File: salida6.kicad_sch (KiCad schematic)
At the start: 7 parts

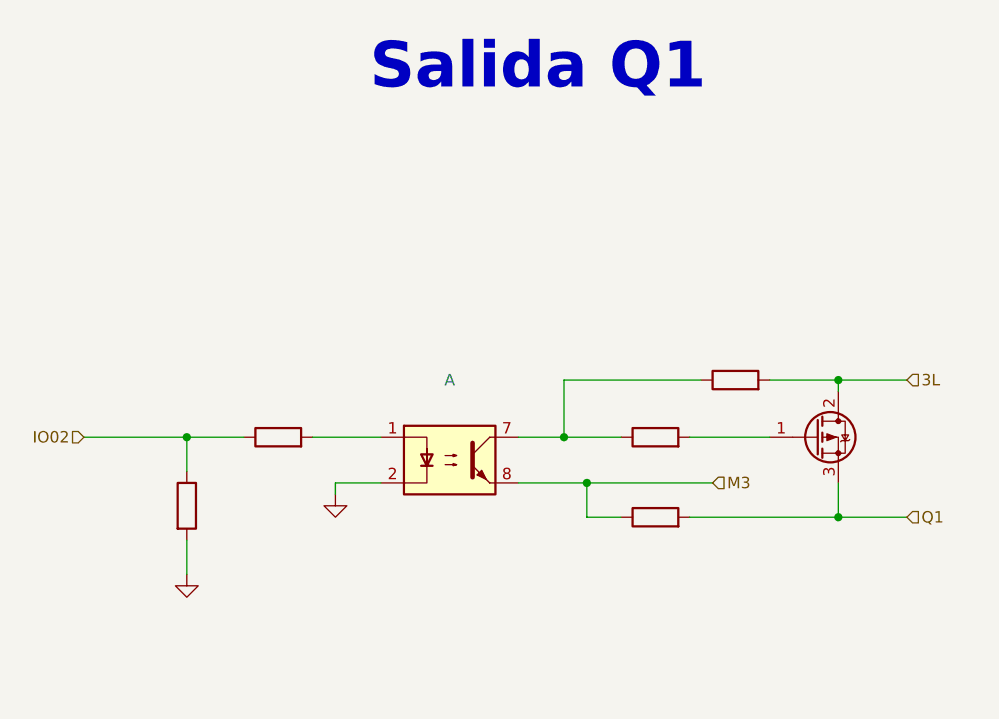
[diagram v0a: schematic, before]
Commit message: add salidas separadas 4,5,6
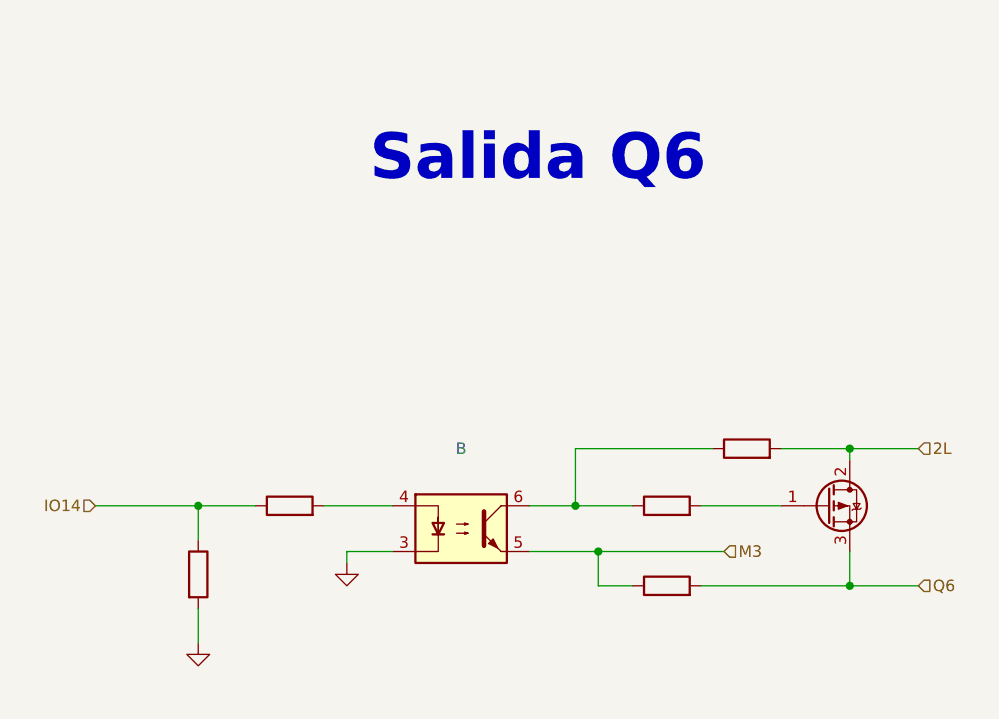
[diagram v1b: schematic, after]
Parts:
- removed ? (x5): (no value), symbol Device:R
- removed ?: (no value), symbol Transistor_FET:FQP27P06
- removed ?: (no value), symbol Isolator:ILD74
- added ? (x5): (no value), symbol Device:R
- added ?: (no value), symbol Isolator:ILD74
- added ?: (no value), symbol Transistor_FET:FQP27P06
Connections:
- net GND: now also ?.2, ?.3
- net M3: now also ?.1, ?.5
- new net: ?.2, ?.4
- new net: ?.1, ?.1, ?.6
- new net: ?.1 (G), ?.2
- new net 2L: ?.2, ?.2 (D)
- new net IO14: ?.1, ?.1
- new net Q6: ?.2, ?.3 (S)
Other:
- note added: "Salida Q6"
- note removed: "Salida Q1"

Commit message: add entradas separadas
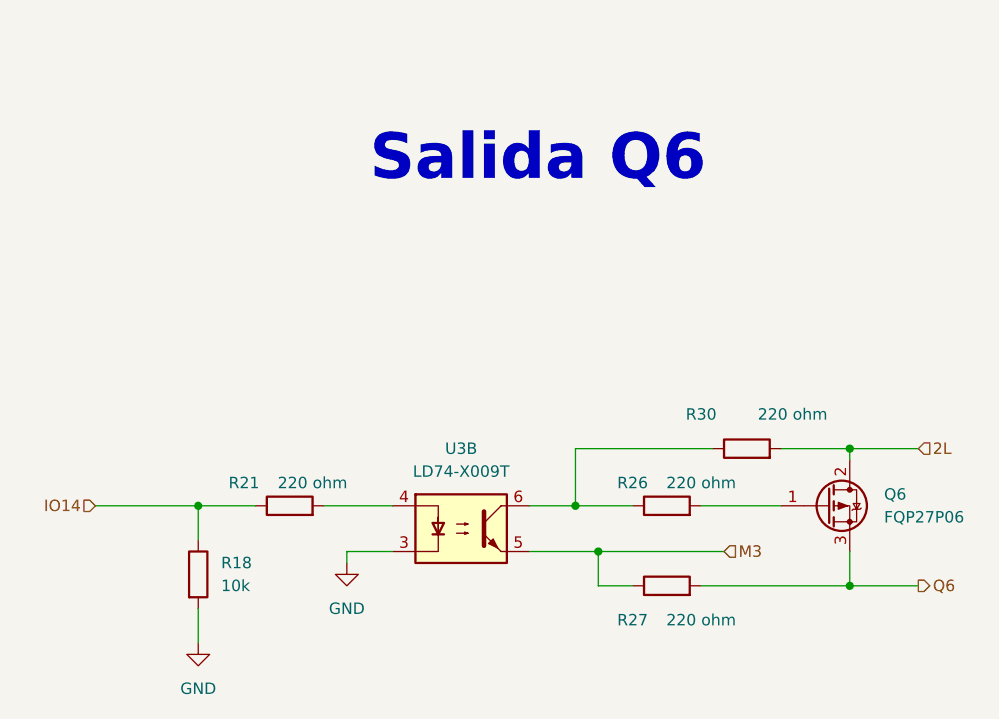
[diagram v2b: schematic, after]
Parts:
- Q6: renamed from ?; value (none) -> FQP27P06; footprint (none) -> Package_TO_SOT_SMD:TO-252-3_TabPin2
- R18: renamed from ?; value (none) -> 10k; footprint (none) -> Resistor_SMD:R_0603_1608Metric
- R21, R26, R27, R30: renamed from ?; value (none) -> 220 ohm; footprint (none) -> Resistor_SMD:R_0603_1608Metric
- U3: renamed from ?; value (none) -> LD74-X009T; footprint (none) -> Package_DIP:DIP-8_W8.89mm_SMDSocket_LongPads
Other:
- title: (none) -> Salida 24 Vdc
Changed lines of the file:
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@@
-(kicad_sch (version 20220929) (generator eeschema)
+(kicad_sch (version 20221004) (generator eeschema)
   (paper "A4" portrait)
+  (title_block
+    (title "Salida 24 Vdc")
+    (date "2022-10-05")
+    (rev "José Luis Laica")
+  )
   (junction (at 142.24 120.65) (diameter 0) (color 0 0 0 0)
   )
@@
     )
   )
-  (hierarchical_label "Q6" (shape input) (at 149.86 135.89 0) (fields_autoplaced)
+  (hierarchical_label "Q6" (shape output) (at 149.86 135.89 0) (fields_autoplaced)
     (effects (font (size 1.27 1.27)) (justify left))
   )
@@
   (symbol (lib_id "Device:R") (at 80.01 127 90) (unit 1)
     (in_bom yes) (on_board yes) (dnp no)
-    (default_instance (reference "") (unit 1) (value "") (footprint ""))
-    (property "Reference" "" (at 74.93 124.46 90)
-      (effects (font (size 1.27 1.27)))
-    )
-    (property "Value" "" (at 82.55 124.46 90)
-      (effects (font (size 1.27 1.27)))
-    )
-    (property "Footprint" "" (at 80.01 128.778 90)
+    (property "Reference" "R21" (at 74.93 124.46 90)
+      (effects (font (size 1.27 1.27)))
+    )
+    (property "Value" "220 ohm" (at 82.55 124.46 90)
+      (effects (font (size 1.27 1.27)))
+    )
+    (property "Footprint" "Resistor_SMD:R_0603_1608Metric" (at 80.01 128.778 90)
       (effects (font (size 1.27 1.27)) hide)
     )
@@
     (pin "1")
     (pin "2")
+    (instances
+      (project "PLC 32 V2"
+        (path "/d17a54f1-6eda-453f-95e1-42a53b02a1c3/4109c560-1e4d-481f-b3b5-bb77ed9700b9"
+          (reference "R21") (unit 1) (value "220 ohm") (footprint "Resistor_SMD:R_0603_1608Metric")
+        )
+      )
+    )
   )
   (symbol (lib_id "Isolator:ILD74") (at 99.06 129.54 0) (unit 2)
     (in_bom yes) (on_board yes) (dnp no) (fields_autoplaced)
-    (default_instance (reference "") (unit 1) (value "") (footprint ""))
-    (property "Reference" "" (at 99.06 120.65 0)
-      (effects (font (size 1.27 1.27)))
-    )
-    (property "Value" "" (at 99.06 123.19 0)
-      (effects (font (size 1.27 1.27)))
-    )
-    (property "Footprint" "" (at 93.98 134.62 0)
+    (property "Reference" "U3" (at 99.06 120.65 0)
+      (effects (font (size 1.27 1.27)))
+    )
+    (property "Value" "LD74-X009T" (at 99.06 123.19 0)
+      (effects (font (size 1.27 1.27)))
+    )
+    (property "Footprint" "Package_DIP:DIP-8_W8.89mm_SMDSocket_LongPads" (at 93.98 134.62 0)
       (effects (font (size 1.27 1.27) italic) (justify left) hide)
     )
@@
     (pin "5")
     (pin "6")
+    (instances
+      (project "PLC 32 V2"
+        (path "/d17a54f1-6eda-453f-95e1-42a53b02a1c3/4109c560-1e4d-481f-b3b5-bb77ed9700b9"
+          (reference "U3") (unit 2) (value "LD74-X009T") (footprint "Package_DIP:DIP-8_W8.89mm_SMDSocket_LongPads")
+        )
+      )
+    )
   )
   (symbol (lib_id "Device:R") (at 121.92 135.89 90) (unit 1)
     (in_bom yes) (on_board yes) (dnp no)
-    (default_instance (reference "") (unit 1) (value "") (footprint ""))
-    (property "Reference" "" (at 118.11 139.7 90)
-      (effects (font (size 1.27 1.27)))
-    )
-    (property "Value" "" (at 125.73 139.7 90)
-      (effects (font (size 1.27 1.27)))
-    )
-    (property "Footprint" "" (at 121.92 137.668 90)
+    (property "Reference" "R27" (at 118.11 139.7 90)
+      (effects (font (size 1.27 1.27)))
+    )
+    (property "Value" "220 ohm" (at 125.73 139.7 90)
+      (effects (font (size 1.27 1.27)))
+    )
+    (property "Footprint" "Resistor_SMD:R_0603_1608Metric" (at 121.92 137.668 90)
       (effects (font (size 1.27 1.27)) hide)
     )
@@
     (pin "1")
     (pin "2")
+    (instances
+      (project "PLC 32 V2"
+        (path "/d17a54f1-6eda-453f-95e1-42a53b02a1c3/4109c560-1e4d-481f-b3b5-bb77ed9700b9"
+          (reference "R27") (unit 1) (value "220 ohm") (footprint "Resistor_SMD:R_0603_1608Metric")
+        )
+      )
+    )
   )
   (symbol (lib_id "Device:R") (at 121.92 127 90) (unit 1)
     (in_bom yes) (on_board yes) (dnp no)
-    (default_instance (reference "") (unit 1) (value "") (footprint ""))
-    (property "Reference" "" (at 118.11 124.46 90)
-      (effects (font (size 1.27 1.27)))
-    )
-    (property "Value" "" (at 125.73 124.46 90)
-      (effects (font (size 1.27 1.27)))
-    )
-    (property "Footprint" "" (at 121.92 128.778 90)
+    (property "Reference" "R26" (at 118.11 124.46 90)
+      (effects (font (size 1.27 1.27)))
+    )
+    (property "Value" "220 ohm" (at 125.73 124.46 90)
+      (effects (font (size 1.27 1.27)))
+    )
+    (property "Footprint" "Resistor_SMD:R_0603_1608Metric" (at 121.92 128.778 90)
       (effects (font (size 1.27 1.27)) hide)
     )
@@
     (pin "1")
     (pin "2")
+    (instances
+      (project "PLC 32 V2"
+        (path "/d17a54f1-6eda-453f-95e1-42a53b02a1c3/4109c560-1e4d-481f-b3b5-bb77ed9700b9"
+          (reference "R26") (unit 1) (value "220 ohm") (footprint "Resistor_SMD:R_0603_1608Metric")
+        )
+      )
+    )
   )
   (symbol (lib_id "power:GND") (at 69.85 142.24 0) (unit 1)
     (in_bom yes) (on_board yes) (dnp no) (fields_autoplaced)
-    (default_instance (reference "") (unit 1) (value "") (footprint ""))
-    (property "Reference" "" (at 69.85 148.59 0)
-      (effects (font (size 1.27 1.27)) hide)
-    )
-    (property "Value" "" (at 69.85 147.32 0)
+    (property "Reference" "#PWR013" (at 69.85 148.59 0)
+      (effects (font (size 1.27 1.27)) hide)
+    )
+    (property "Value" "GND" (at 69.85 147.32 0)
       (effects (font (size 1.27 1.27)))
     )
@@
     )
     (pin "1")
+    (instances
+      (project "PLC 32 V2"
+        (path "/d17a54f1-6eda-453f-95e1-42a53b02a1c3/4109c560-1e4d-481f-b3b5-bb77ed9700b9"
+          (reference "#PWR013") (unit 1) (value "GND") (footprint "")
+        )
+      )
+    )
   )
   (symbol (lib_id "Device:R") (at 69.85 134.62 0) (unit 1)
     (in_bom yes) (on_board yes) (dnp no) (fields_autoplaced)
-    (default_instance (reference "") (unit 1) (value "") (footprint ""))
-    (property "Reference" "" (at 72.39 133.3499 0)
-      (effects (font (size 1.27 1.27)) (justify left))
-    )
-    (property "Value" "" (at 72.39 135.8899 0)
-      (effects (font (size 1.27 1.27)) (justify left))
-    )
-    (property "Footprint" "" (at 68.072 134.62 90)
+    (property "Reference" "R18" (at 72.39 133.3499 0)
+      (effects (font (size 1.27 1.27)) (justify left))
+    )
+    (property "Value" "10k" (at 72.39 135.8899 0)
+      (effects (font (size 1.27 1.27)) (justify left))
+    )
+    (property "Footprint" "Resistor_SMD:R_0603_1608Metric" (at 68.072 134.62 90)
       (effects (font (size 1.27 1.27)) hide)
     )
@@
     (pin "1")
     (pin "2")
+    (instances
+      (project "PLC 32 V2"
+        (path "/d17a54f1-6eda-453f-95e1-42a53b02a1c3/4109c560-1e4d-481f-b3b5-bb77ed9700b9"
+          (reference "R18") (unit 1) (value "10k") (footprint "Resistor_SMD:R_0603_1608Metric")
+        )
+      )
+    )
   )
   (symbol (lib_id "power:GND") (at 86.36 133.35 0) (unit 1)
     (in_bom yes) (on_board yes) (dnp no) (fields_autoplaced)
-    (default_instance (reference "") (unit 1) (value "") (footprint ""))
-    (property "Reference" "" (at 86.36 139.7 0)
-      (effects (font (size 1.27 1.27)) hide)
-    )
-    (property "Value" "" (at 86.36 138.43 0)
+    (property "Reference" "#PWR016" (at 86.36 139.7 0)
+      (effects (font (size 1.27 1.27)) hide)
+    )
+    (property "Value" "GND" (at 86.36 138.43 0)
       (effects (font (size 1.27 1.27)))
     )
@@
     )
     (pin "1")
+    (instances
+      (project "PLC 32 V2"
+        (path "/d17a54f1-6eda-453f-95e1-42a53b02a1c3/4109c560-1e4d-481f-b3b5-bb77ed9700b9"
+          (reference "#PWR016") (unit 1) (value "GND") (footprint "")
+        )
+      )
+    )
   )
   (symbol (lib_id "Device:R") (at 130.81 120.65 90) (unit 1)
     (in_bom yes) (on_board yes) (dnp no)
-    (default_instance (reference "") (unit 1) (value "") (footprint ""))
-    (property "Reference" "" (at 125.73 116.84 90)
-      (effects (font (size 1.27 1.27)))
-    )
-    (property "Value" "" (at 135.89 116.84 90)
-      (effects (font (size 1.27 1.27)))
-    )
-    (property "Footprint" "" (at 130.81 122.428 90)
+    (property "Reference" "R30" (at 125.73 116.84 90)
+      (effects (font (size 1.27 1.27)))
+    )
+    (property "Value" "220 ohm" (at 135.89 116.84 90)
+      (effects (font (size 1.27 1.27)))
+    )
+    (property "Footprint" "Resistor_SMD:R_0603_1608Metric" (at 130.81 122.428 90)
       (effects (font (size 1.27 1.27)) hide)
     )
@@
     (pin "1")
     (pin "2")
+    (instances
+      (project "PLC 32 V2"
+        (path "/d17a54f1-6eda-453f-95e1-42a53b02a1c3/4109c560-1e4d-481f-b3b5-bb77ed9700b9"
+          (reference "R30") (unit 1) (value "220 ohm") (footprint "Resistor_SMD:R_0603_1608Metric")
+        )
+      )
+    )
   )
   (symbol (lib_id "Transistor_FET:FQP27P06") (at 139.7 127 0) (unit 1)
     (in_bom yes) (on_board yes) (dnp no) (fields_autoplaced)
-    (default_instance (reference "") (unit 1) (value "") (footprint ""))
-    (property "Reference" "" (at 146.05 125.7299 0)
-      (effects (font (size 1.27 1.27)) (justify left))
-    )
-    (property "Value" "" (at 146.05 128.2699 0)
-      (effects (font (size 1.27 1.27)) (justify left))
-    )
-    (property "Footprint" "" (at 144.78 128.905 0)
+    (property "Reference" "Q6" (at 146.05 125.7299 0)
+      (effects (font (size 1.27 1.27)) (justify left))
+    )
+    (property "Value" "FQP27P06" (at 146.05 128.2699 0)
+      (effects (font (size 1.27 1.27)) (justify left))
+    )
+    (property "Footprint" "Package_TO_SOT_SMD:TO-252-3_TabPin2" (at 144.78 128.905 0)
       (effects (font (size 1.27 1.27) italic) (justify left) hide)
     )
@@
     (pin "2")
     (pin "3")
+    (instances
+      (project "PLC 32 V2"
+        (path "/d17a54f1-6eda-453f-95e1-42a53b02a1c3/4109c560-1e4d-481f-b3b5-bb77ed9700b9"
+          (reference "Q6") (unit 1) (value "FQP27P06") (footprint "Package_TO_SOT_SMD:TO-252-3_TabPin2")
+        )
+      )
+    )
   )
 )

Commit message: input/output separadas
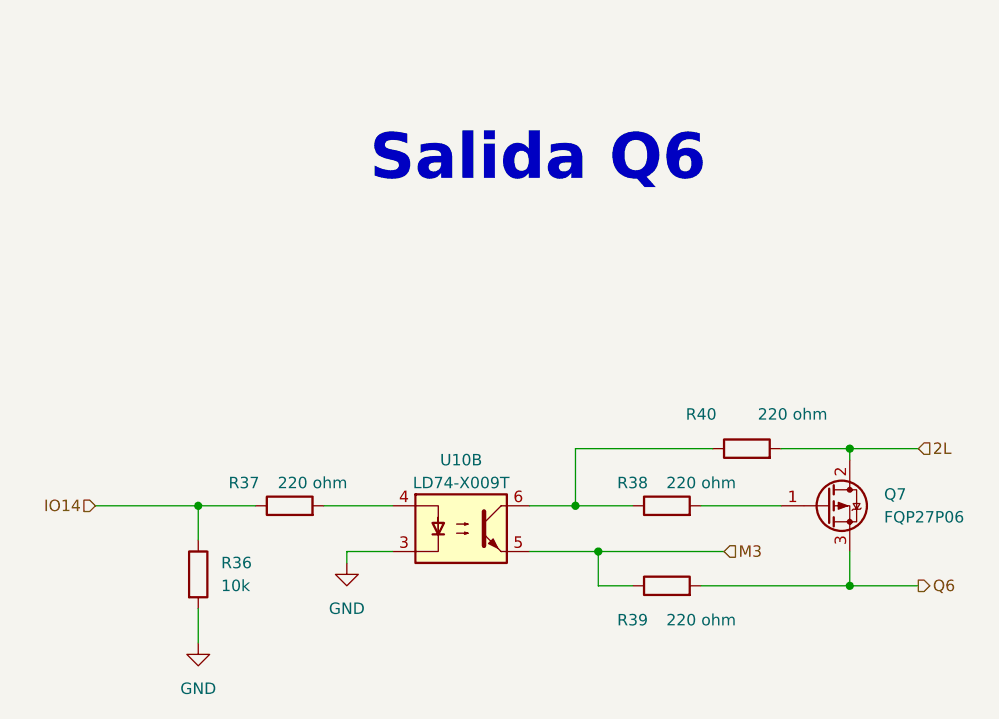
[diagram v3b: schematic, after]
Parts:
- renumbered Q6 to Q7, R18 to R36, R21 to R37, R26 to R38, R27 to R39, R30 to R40, U3 to U10
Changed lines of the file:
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@@
   (title_block
     (title "Salida 24 Vdc")
-    (date "2022-10-05")
+    (date "2022-10-09")
     (rev "José Luis Laica")
   )
@@
   (symbol (lib_id "Device:R") (at 80.01 127 90) (unit 1)
     (in_bom yes) (on_board yes) (dnp no)
-    (property "Reference" "R21" (at 74.93 124.46 90)
+    (property "Reference" "R37" (at 74.93 124.46 90)
       (effects (font (size 1.27 1.27)))
     )
@@
       (project "PLC 32 V2"
         (path "/d17a54f1-6eda-453f-95e1-42a53b02a1c3/4109c560-1e4d-481f-b3b5-bb77ed9700b9"
-          (reference "R21") (unit 1) (value "220 ohm") (footprint "Resistor_SMD:R_0603_1608Metric")
+          (reference "R37") (unit 1) (value "220 ohm") (footprint "Resistor_SMD:R_0603_1608Metric")
         )
       )
@@
   (symbol (lib_id "Isolator:ILD74") (at 99.06 129.54 0) (unit 2)
     (in_bom yes) (on_board yes) (dnp no) (fields_autoplaced)
-    (property "Reference" "U3" (at 99.06 120.65 0)
-      (effects (font (size 1.27 1.27)))
-    )
-    (property "Value" "LD74-X009T" (at 99.06 123.19 0)
+    (property "Reference" "U10" (at 99.06 121.92 0)
+      (effects (font (size 1.27 1.27)))
+    )
+    (property "Value" "LD74-X009T" (at 99.06 124.46 0)
       (effects (font (size 1.27 1.27)))
     )
@@
       (project "PLC 32 V2"
         (path "/d17a54f1-6eda-453f-95e1-42a53b02a1c3/4109c560-1e4d-481f-b3b5-bb77ed9700b9"
-          (reference "U3") (unit 2) (value "LD74-X009T") (footprint "Package_DIP:DIP-8_W8.89mm_SMDSocket_LongPads")
+          (reference "U10") (unit 2) (value "LD74-X009T") (footprint "Package_DIP:DIP-8_W8.89mm_SMDSocket_LongPads")
         )
       )
@@
   (symbol (lib_id "Device:R") (at 121.92 135.89 90) (unit 1)
     (in_bom yes) (on_board yes) (dnp no)
-    (property "Reference" "R27" (at 118.11 139.7 90)
+    (property "Reference" "R39" (at 118.11 139.7 90)
       (effects (font (size 1.27 1.27)))
     )
@@
       (project "PLC 32 V2"
         (path "/d17a54f1-6eda-453f-95e1-42a53b02a1c3/4109c560-1e4d-481f-b3b5-bb77ed9700b9"
-          (reference "R27") (unit 1) (value "220 ohm") (footprint "Resistor_SMD:R_0603_1608Metric")
+          (reference "R39") (unit 1) (value "220 ohm") (footprint "Resistor_SMD:R_0603_1608Metric")
         )
       )
@@
   (symbol (lib_id "Device:R") (at 121.92 127 90) (unit 1)
     (in_bom yes) (on_board yes) (dnp no)
-    (property "Reference" "R26" (at 118.11 124.46 90)
+    (property "Reference" "R38" (at 118.11 124.46 90)
       (effects (font (size 1.27 1.27)))
     )
@@
       (project "PLC 32 V2"
         (path "/d17a54f1-6eda-453f-95e1-42a53b02a1c3/4109c560-1e4d-481f-b3b5-bb77ed9700b9"
-          (reference "R26") (unit 1) (value "220 ohm") (footprint "Resistor_SMD:R_0603_1608Metric")
+          (reference "R38") (unit 1) (value "220 ohm") (footprint "Resistor_SMD:R_0603_1608Metric")
         )
       )
@@
   (symbol (lib_id "power:GND") (at 69.85 142.24 0) (unit 1)
     (in_bom yes) (on_board yes) (dnp no) (fields_autoplaced)
-    (property "Reference" "#PWR013" (at 69.85 148.59 0)
+    (property "Reference" "#PWR022" (at 69.85 148.59 0)
       (effects (font (size 1.27 1.27)) hide)
     )
@@
       (project "PLC 32 V2"
         (path "/d17a54f1-6eda-453f-95e1-42a53b02a1c3/4109c560-1e4d-481f-b3b5-bb77ed9700b9"
-          (reference "#PWR013") (unit 1) (value "GND") (footprint "")
+          (reference "#PWR022") (unit 1) (value "GND") (footprint "")
         )
       )
@@
   (symbol (lib_id "Device:R") (at 69.85 134.62 0) (unit 1)
     (in_bom yes) (on_board yes) (dnp no) (fields_autoplaced)
-    (property "Reference" "R18" (at 72.39 133.3499 0)
+    (property "Reference" "R36" (at 72.39 133.3499 0)
       (effects (font (size 1.27 1.27)) (justify left))
     )
@@
       (project "PLC 32 V2"
         (path "/d17a54f1-6eda-453f-95e1-42a53b02a1c3/4109c560-1e4d-481f-b3b5-bb77ed9700b9"
-          (reference "R18") (unit 1) (value "10k") (footprint "Resistor_SMD:R_0603_1608Metric")
+          (reference "R36") (unit 1) (value "10k") (footprint "Resistor_SMD:R_0603_1608Metric")
         )
       )
@@
   (symbol (lib_id "power:GND") (at 86.36 133.35 0) (unit 1)
     (in_bom yes) (on_board yes) (dnp no) (fields_autoplaced)
-    (property "Reference" "#PWR016" (at 86.36 139.7 0)
+    (property "Reference" "#PWR023" (at 86.36 139.7 0)
       (effects (font (size 1.27 1.27)) hide)
     )
@@
       (project "PLC 32 V2"
         (path "/d17a54f1-6eda-453f-95e1-42a53b02a1c3/4109c560-1e4d-481f-b3b5-bb77ed9700b9"
-          (reference "#PWR016") (unit 1) (value "GND") (footprint "")
+          (reference "#PWR023") (unit 1) (value "GND") (footprint "")
         )
       )
@@
   (symbol (lib_id "Device:R") (at 130.81 120.65 90) (unit 1)
     (in_bom yes) (on_board yes) (dnp no)
-    (property "Reference" "R30" (at 125.73 116.84 90)
+    (property "Reference" "R40" (at 125.73 116.84 90)
       (effects (font (size 1.27 1.27)))
     )
@@
       (project "PLC 32 V2"
         (path "/d17a54f1-6eda-453f-95e1-42a53b02a1c3/4109c560-1e4d-481f-b3b5-bb77ed9700b9"
-          (reference "R30") (unit 1) (value "220 ohm") (footprint "Resistor_SMD:R_0603_1608Metric")
+          (reference "R40") (unit 1) (value "220 ohm") (footprint "Resistor_SMD:R_0603_1608Metric")
         )
       )
@@
   (symbol (lib_id "Transistor_FET:FQP27P06") (at 139.7 127 0) (unit 1)
     (in_bom yes) (on_board yes) (dnp no) (fields_autoplaced)
-    (property "Reference" "Q6" (at 146.05 125.7299 0)
+    (property "Reference" "Q7" (at 146.05 125.7299 0)
       (effects (font (size 1.27 1.27)) (justify left))
     )
@@
       (project "PLC 32 V2"
         (path "/d17a54f1-6eda-453f-95e1-42a53b02a1c3/4109c560-1e4d-481f-b3b5-bb77ed9700b9"
-          (reference "Q6") (unit 1) (value "FQP27P06") (footprint "Package_TO_SOT_SMD:TO-252-3_TabPin2")
-        )
-      )
+          (reference "Q7") (unit 1) (value "FQP27P06") (footprint "Package_TO_SOT_SMD:TO-252-3_TabPin2")
+        )
+      )
